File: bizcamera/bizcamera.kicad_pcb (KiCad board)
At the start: 2 copper layers, 84.5 x 55 mm, 0 parts

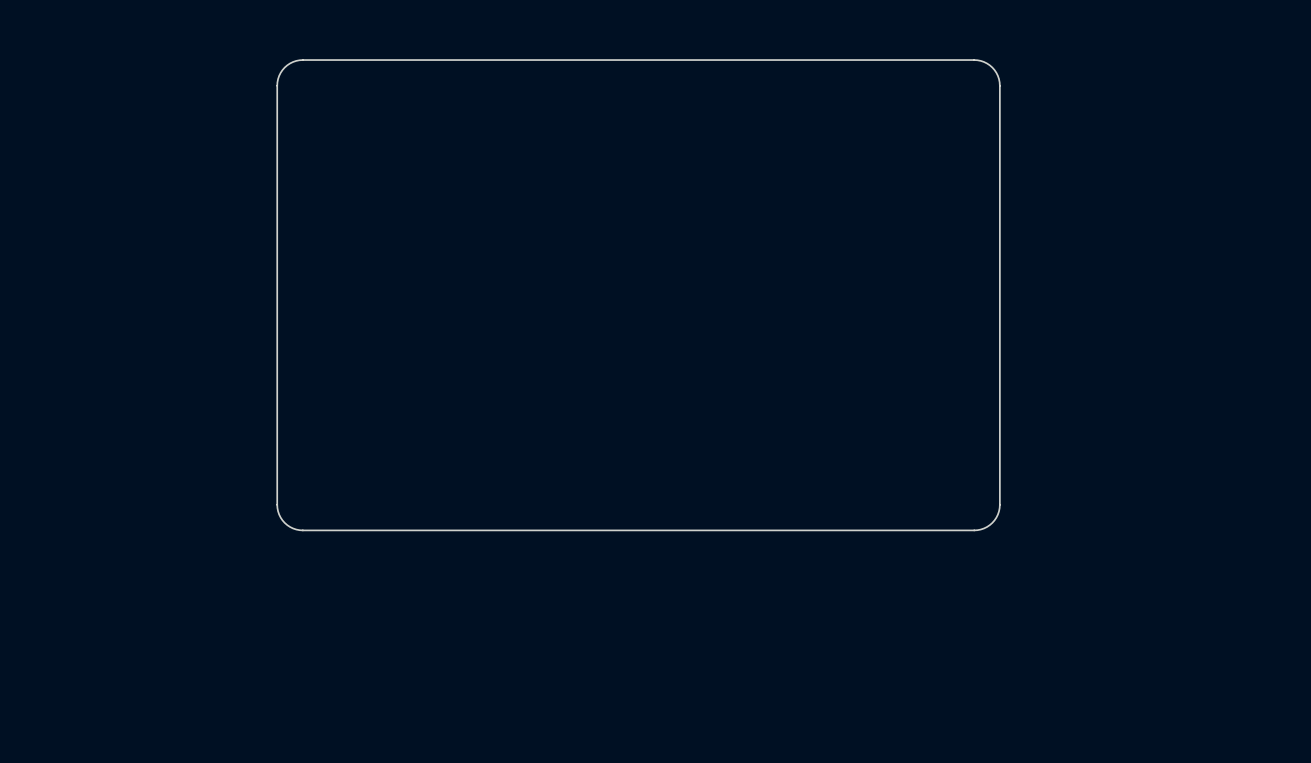
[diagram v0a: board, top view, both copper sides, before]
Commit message: Schematic rev1
Rev1 of the schematic, not finished, but close.

Switched to rp2350 because PIO is powerful enough to grab frames without DCMI iface
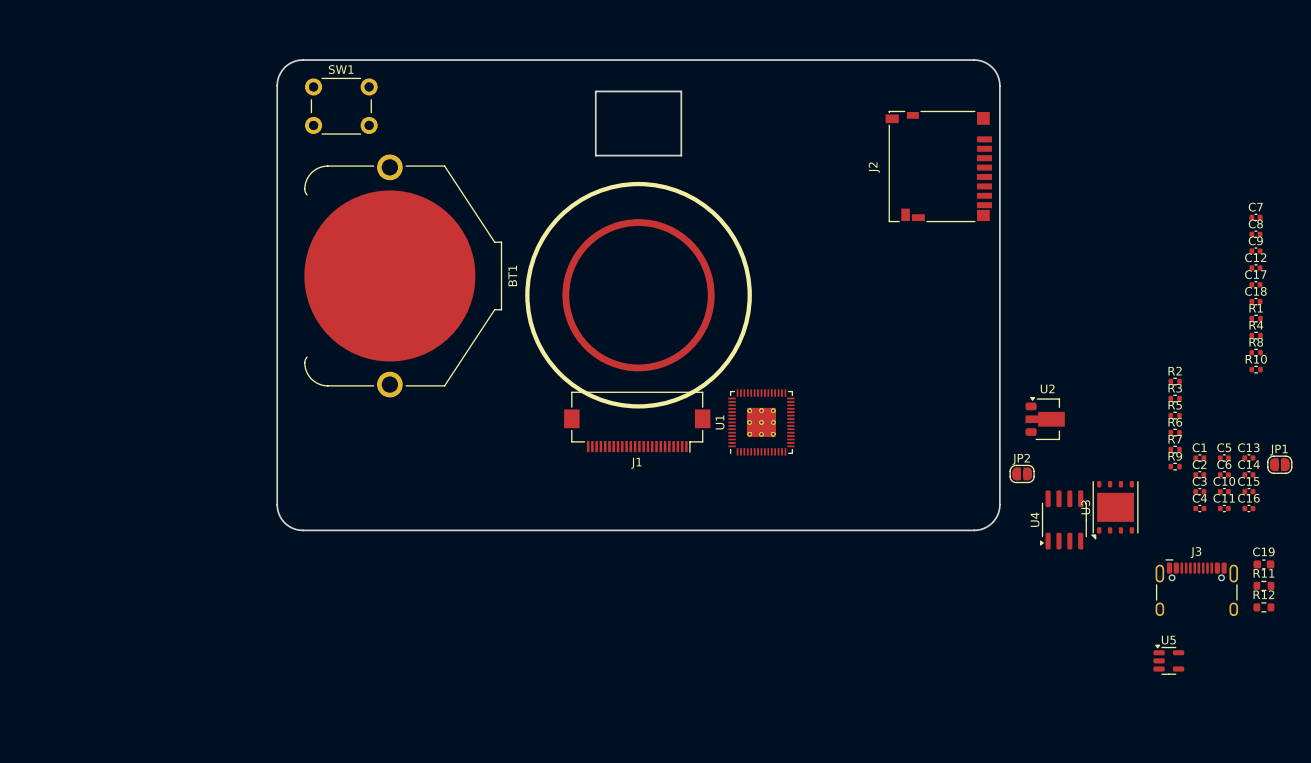
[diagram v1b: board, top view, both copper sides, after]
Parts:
- added BT1: CR2032, Battery:BatteryHolder_Keystone_3009_1x2450, F.Cu at (124.7, 90.2)
- added C1: 100n, Capacitor_SMD:C_0402_1005Metric, F.Cu at (219.4, 111.5)
- added C10: 100n, Capacitor_SMD:C_0402_1005Metric, F.Cu at (222.2, 115.5)
- added C11: 100n, Capacitor_SMD:C_0402_1005Metric, F.Cu at (222.2, 117.4)
- added C12: 4.7u, Capacitor_SMD:C_0402_1005Metric, F.Cu at (225.9, 89.3)
- added C13: 100n, Capacitor_SMD:C_0402_1005Metric, F.Cu at (225.1, 111.5)
- added C14: 100n, Capacitor_SMD:C_0402_1005Metric, F.Cu at (225.1, 113.5)
- added C15: 100n, Capacitor_SMD:C_0402_1005Metric, F.Cu at (225.1, 115.5)
- added C16: 100n, Capacitor_SMD:C_0402_1005Metric, F.Cu at (225.1, 117.4)
- added C17: 15p, Capacitor_SMD:C_0402_1005Metric, F.Cu at (225.9, 91.3)
- added C18: 15p, Capacitor_SMD:C_0402_1005Metric, F.Cu at (225.9, 93.2)
- added C19: 10u, Capacitor_SMD:C_0603_1608Metric, F.Cu at (226.9, 124.0)
- added C2: 100n, Capacitor_SMD:C_0402_1005Metric, F.Cu at (219.4, 113.5)
- added C3: 100n, Capacitor_SMD:C_0402_1005Metric, F.Cu at (219.4, 115.5)
- added C4: 100n, Capacitor_SMD:C_0402_1005Metric, F.Cu at (219.4, 117.4)
- added C5: 100n, Capacitor_SMD:C_0402_1005Metric, F.Cu at (222.2, 111.5)
- added C6: 100n, Capacitor_SMD:C_0402_1005Metric, F.Cu at (222.2, 113.5)
- added C7: 4.7u, Capacitor_SMD:C_0402_1005Metric, F.Cu at (225.9, 83.4)
- added C8: 4.7u, Capacitor_SMD:C_0402_1005Metric, F.Cu at (225.9, 85.4)
- added C9: 4.7u, Capacitor_SMD:C_0402_1005Metric, F.Cu at (225.9, 87.3)
- added J1: Camera, Connector_FFC-FPC:Hirose_FH12-24S-0.5SH_1x24-1MP_P0.50mm_Horizontal, F.Cu at (153.6, 108.3)
- added J2: Micro_SD_Card_Det1, Connector_Card:microSD_HC_Hirose_DM3D-SF, F.Cu at (188.8, 77.5)
- added J3: USB_C_Receptacle_USB2.0_14P, Connector_USB:USB_C_Receptacle_HCTL_HC-TYPE-C-16P-01A, F.Cu at (219.0, 128.2)
- added JP1: USB_BOOT, Jumper:SolderJumper-2_P1.3mm_Open_RoundedPad1.0x1.5mm, F.Cu at (228.7, 112.3)
- added JP2: USB_BOOT, Jumper:SolderJumper-2_P1.3mm_Open_RoundedPad1.0x1.5mm, F.Cu at (198.6, 113.4)
- added R1: 33, Resistor_SMD:R_0402_1005Metric, F.Cu at (226.0, 95.2)
- added R10: 10k, Resistor_SMD:R_0402_1005Metric, F.Cu at (226.0, 101.2)
- added R11: 5.1k, Resistor_SMD:R_0603_1608Metric, F.Cu at (226.9, 126.5)
- added R12: 5.1k, Resistor_SMD:R_0603_1608Metric, F.Cu at (226.9, 129.0)
- added R2: R, Resistor_SMD:R_0402_1005Metric, F.Cu at (216.5, 102.6)
- added R3: R, Resistor_SMD:R_0402_1005Metric, F.Cu at (216.5, 104.6)
- added R4: 1k, Resistor_SMD:R_0402_1005Metric, F.Cu at (226.0, 97.2)
- added R5: 0, Resistor_SMD:R_0402_1005Metric, F.Cu at (216.5, 106.6)
- added R6: 0, Resistor_SMD:R_0402_1005Metric, F.Cu at (216.5, 108.6)
- added R7: DNF, Resistor_SMD:R_0402_1005Metric, F.Cu at (216.5, 110.5)
- added R8: 1k, Resistor_SMD:R_0402_1005Metric, F.Cu at (226.0, 99.2)
- added R9: 0, Resistor_SMD:R_0402_1005Metric, F.Cu at (216.5, 112.5)
- added SW1: SW_Push, Button_Switch_THT:SW_PUSH_6mm_H4.3mm, F.Cu at (115.8, 68.2)
- added U1: RP2350_60QFN, RP2350A:RP2350-QFN-60-1EP_7x7_P0.4mm_EP3.4x3.4mm_ThermalVias, F.Cu at (168.1, 107.4)
- added U2: MCP1703Ax-180xxMB, Package_TO_SOT_SMD:SOT-89-3, F.Cu at (201.6, 107.0)
- added U3: W25Q128JVP, Package_SON:WSON-8-1EP_6x5mm_P1.27mm_EP3.4x4.3mm, F.Cu at (209.5, 117.3)
- added U4: ESP-PSRAM32, Package_SO:SOIC-8_3.9x4.9mm_P1.27mm, F.Cu at (203.5, 118.8)
- added U5: SPX3819M5-L-3-3, Package_TO_SOT_SMD:SOT-23-5, F.Cu at (215.8, 135.3)
- added kibuzzard-6812137D: G***, kibuzzard-6812137D, B.Cu at (171.9, 72.8)
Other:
- outline, holes or cut-outs redrawn

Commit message: Finish schematic
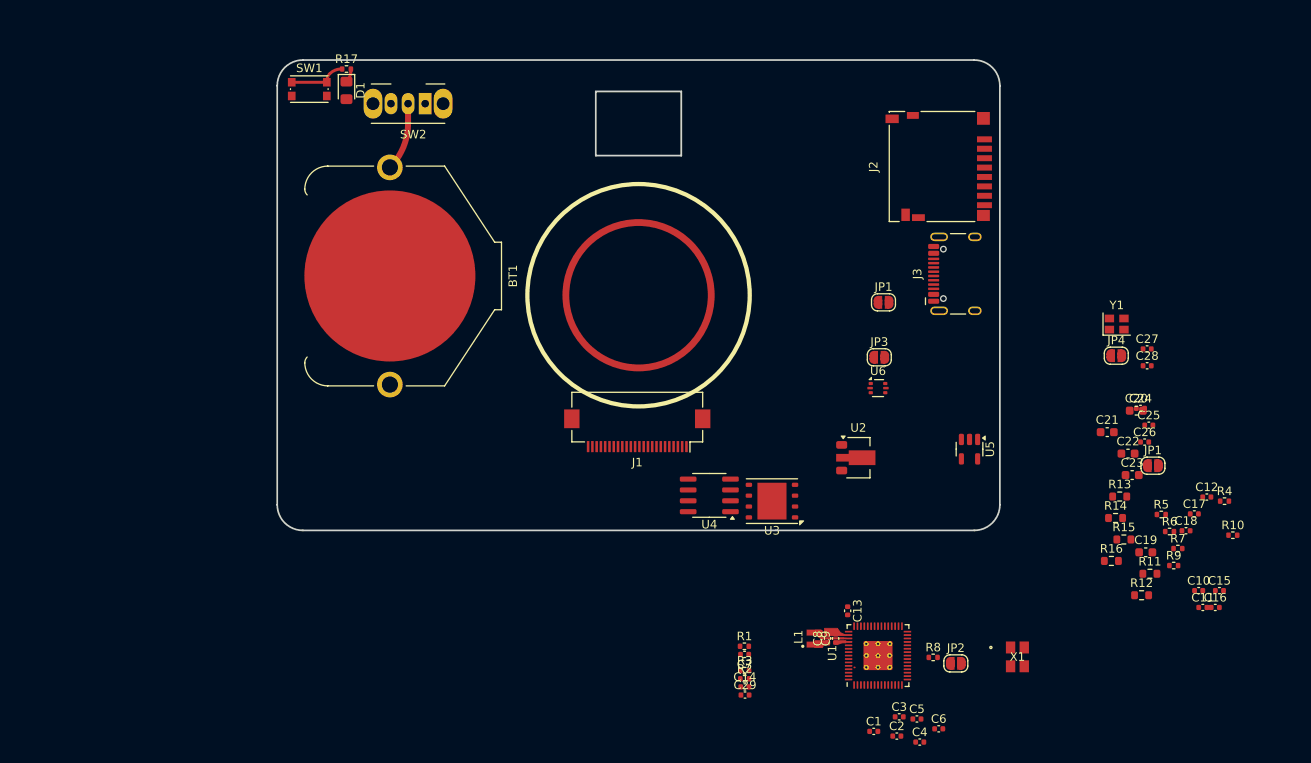
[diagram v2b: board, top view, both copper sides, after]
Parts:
- added C20: 10u, Capacitor_SMD:C_0603_1608Metric, F.Cu at (212.0, 106.0)
- added C21: 10u, Capacitor_SMD:C_0603_1608Metric, F.Cu at (208.6, 108.5)
- added C22: 10u, Capacitor_SMD:C_0603_1608Metric, F.Cu at (211.0, 111.0)
- added C23: 10u, Capacitor_SMD:C_0603_1608Metric, F.Cu at (211.5, 113.5)
- added C24: 100n, Capacitor_SMD:C_0402_1005Metric, F.Cu at (212.4, 105.7)
- added C25: 100n, Capacitor_SMD:C_0402_1005Metric, F.Cu at (213.4, 107.7)
- added C26: 15p, Capacitor_SMD:C_0402_1005Metric, F.Cu at (212.9, 109.7)
- added C27: 100n, Capacitor_SMD:C_0402_1005Metric, F.Cu at (213.2, 98.8)
- added C28: 100n, Capacitor_SMD:C_0402_1005Metric, F.Cu at (213.2, 100.8)
- added C29: 100n, Capacitor_SMD:C_0402_1005Metric, F.Cu at (166.2, 139.2)
- added D1: LED, LED_SMD:LED_0805_2012Metric_Pad1.15x1.40mm_HandSolder, F.Cu at (119.6, 68.5)
- added JP1: CAM_AF, Jumper:SolderJumper-2_P1.3mm_Open_RoundedPad1.0x1.5mm, F.Cu at (213.9, 112.4)
- added JP3: DVDD_1V8, Jumper:SolderJumper-2_P1.3mm_Open_RoundedPad1.0x1.5mm, F.Cu at (181.9, 99.8)
- added JP4: XTAL_JMP, Jumper:SolderJumper-2_P1.3mm_Open_RoundedPad1.0x1.5mm, F.Cu at (209.6, 99.6)
- added L1: 3.3u, RP2350A:L_pol_2016, F.Cu at (174.2, 132.7)
- added R13: 10K, Resistor_SMD:R_0603_1608Metric, F.Cu at (210.0, 116.0)
- added R14: 10K, Resistor_SMD:R_0603_1608Metric, F.Cu at (209.5, 118.5)
- added R15: 10K, Resistor_SMD:R_0603_1608Metric, F.Cu at (210.5, 121.1)
- added R16: 10K, Resistor_SMD:R_0603_1608Metric, F.Cu at (209.0, 123.6)
- added R17: 1k, Resistor_SMD:R_0402_1005Metric, F.Cu at (119.6, 66.0)
- added SW2: SW_SPDT, Button_Switch_THT:SW_Slide_SPDT_Angled_CK_OS102011MA1Q, F.Cu at (128.8, 70.1)
- added U6: USBLC6-2P6, Package_TO_SOT_SMD:SOT-666, F.Cu at (181.8, 103.4)
- added X1: ABM8-272-T3, ABM8_272_T3:ABM8-272-T3_ABR, F.Cu at (198.0, 134.8)
- added Y1: SG-210STF 24.0ML0, Oscillator:Oscillator_SMD_SeikoEpson_SG210-4Pin_2.5x2.0mm, F.Cu at (209.7, 95.9)
- C18: value 15p -> 12p
- J3: value USB_C_Receptacle_USB2.0_14P -> USB_IN
- JP1: value USB_BOOT -> CAM_AF
- R2, R3: value R -> 0
- R7: value DNF -> 10k
- SW1: value SW_Push -> USB_BOOT; footprint Button_Switch_THT:SW_PUSH_6mm_H4.3mm -> Button_Switch_SMD:SW_Push_1P1T_NO_CK_KMR2
- moved C7 78.7 mm to (166.2, 134.5), turned to 180 degrees
- moved R1 71.0 mm to (166.1, 133.6)
- moved C8 68.9 mm to (175.8, 132.6), turned to 90 degrees
- moved C9 66.8 mm to (176.8, 132.6), turned to 90 degrees
- moved C14 63.9 mm to (166.2, 138.3)
- moved R2 61.2 mm to (166.2, 137.3)
- moved R3 59.5 mm to (166.2, 136.4)
- moved R8 51.9 mm to (188.2, 134.8)
- moved C13 50.2 mm to (178.2, 129.4), turned to -90 degrees
- moved JP1 50.1 mm to (182.4, 93.3)
- moved C1 49.8 mm to (181.2, 143.5)
- moved C5 47.2 mm to (186.3, 142.1)
- moved C2 46.8 mm to (183.9, 144.1)
- moved J3 46.8 mm to (192.0, 90.0), turned to 90 degrees
- moved C6 44.7 mm to (188.8, 143.2)
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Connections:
- BT1 pad 1: +3V3 -> Net-(BT1-+)
- C18 pad 1: unconnected-(C18-Pad1) -> /XIN
- C19 pad 1: +5V -> -BATT
- C19 pad 2: -BATT -> +5V
- J1 pad 12: /MCLK -> /CAM_XTAL
- J1 pad 14: /DOVDD 1.8 -> +1V8
- J1 pad 2: +3V3 -> Net-(J1-Pin_2)
- J3 pad A6: /USB_DP -> Net-(J3-D+-PadA6)
- J3 pad A7: /USB_DM -> Net-(J3-D--PadA7)
- J3 pad B6: /USB_DP -> Net-(J3-D+-PadA6)
- J3 pad B7: /USB_DM -> Net-(J3-D--PadA7)
- JP1 pad 1: -BATT -> +3V3
- JP1 pad 2: /USB_BOOT -> Net-(J1-Pin_2)
- JP2 pad 2: Net-(JP2-B) -> -BATT
- R2 pad 1: Net-(U1-USB_DP) -> /USB_DP
- R3 pad 1: Net-(U1-USB_DM) -> /USB_DN
- R3 pad 2: /USB_DM -> /USB_DN
- R8 pad 1: -BATT -> Net-(U1-RUN)
- R8 pad 2: Net-(JP2-B) -> Net-(JP2-A)
- SW1 pad 1: unconnected-(SW1-Pad1) -> -BATT
- SW1 pad 2: unconnected-(SW1-Pad2) -> /USB_BOOT
- U1 pad 10: unconnected-(U1-GPIO7-Pad10) -> /D3
- U1 pad 12: unconnected-(U1-GPIO8-Pad12) -> /D4/MDN0
- U1 pad 13: unconnected-(U1-GPIO9-Pad13) -> /SDA
- U1 pad 14: unconnected-(U1-GPIO10-Pad14) -> /SCL
- U1 pad 15: unconnected-(U1-GPIO11-Pad15) -> /RST
- U1 pad 16: unconnected-(U1-GPIO12-Pad16) -> /VSYNC
- U1 pad 17: unconnected-(U1-GPIO13-Pad17) -> /HSYNC
- U1 pad 18: unconnected-(U1-GPIO14-Pad18) -> /PCLK
- U1 pad 26: Net-(JP2-A) -> Net-(U1-RUN)
- U1 pad 28: unconnected-(U1-GPIO17-Pad28) -> /XTAL_EN
- U1 pad 3: unconnected-(U1-GPIO1-Pad3) -> /D9/MPD1
- U1 pad 31: unconnected-(U1-GPIO19-Pad31) -> /SD_DET
- U1 pad 32: unconnected-(U1-GPIO20-Pad32) -> /SPI_DO
- U1 pad 33: unconnected-(U1-GPIO21-Pad33) -> /SCLK
- U1 pad 34: unconnected-(U1-GPIO22-Pad34) -> /SPI_DI
- U1 pad 35: unconnected-(U1-GPIO23-Pad35) -> /SPI_CS
- U1 pad 36: unconnected-(U1-GPIO24-Pad36) -> Net-(D1-A)
- U1 pad 4: unconnected-(U1-GPIO2-Pad4) -> /D8/MDN1
- U1 pad 5: unconnected-(U1-GPIO3-Pad5) -> /D7/MCP
- U1 pad 51: Net-(U1-USB_DM) -> /USB_DN
- U1 pad 52: Net-(U1-USB_DP) -> /USB_DP
- U1 pad 54: unconnected-(U1-QSPI_IOVDD-Pad54) -> +3V3
- U1 pad 7: unconnected-(U1-GPIO4-Pad7) -> /D6/MCN
- U1 pad 8: unconnected-(U1-GPIO5-Pad8) -> /D2
- U1 pad 9: unconnected-(U1-GPIO6-Pad9) -> /D5/MDP0
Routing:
- net Net-(BT1-+): track 0.00 -> 7.98 mm
- net -BATT: track 0.00 -> 6.77 mm
- net Net-(D1-K): track 0.00 -> 1.60 mm

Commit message: Near final design
Near final design for prototype model, for both schematic and PCB

Layout was an absolute nightmare. But I think this is the best I can do with the constraints, and it should look pretty nice too.
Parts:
- removed the JP1 at (213.9, 112.4)
- removed SW2: SW_SPDT, Button_Switch_THT:SW_Slide_SPDT_Angled_CK_OS102011MA1Q
- removed kibuzzard-6812137D: G***, kibuzzard-6812137D
- added C30: 10u, Capacitor_SMD:C_0603_1608Metric, F.Cu at (123.5, 112.5)
- added C31: 68u, Capacitor_SMD:C_0603_1608Metric, F.Cu at (129.8, 114.6)
- added C32: 68u, Capacitor_SMD:C_0603_1608Metric, F.Cu at (128.4, 114.6)
- added C33: 10u, Capacitor_SMD:C_0603_1608Metric, F.Cu at (141.5, 113.0)
- added C34: 10u, Capacitor_SMD:C_0603_1608Metric, F.Cu at (140.0, 113.0)
- added C35: 10u, Capacitor_SMD:C_0603_1608Metric, F.Cu at (137.7, 110.5)
- added L2: 1u, Kiyo:TFM201610ALMA, F.Cu at (123.9, 114.6)
- added L3: 1u, Kiyo:TFM201610ALMA, F.Cu at (138.9, 115.9)
- added R18: 10k, Resistor_SMD:R_0402_1005Metric, F.Cu at (185.5, 106.1)
- added R19: 453k, Resistor_SMD:R_0402_1005Metric_Pad0.72x0.64mm_HandSolder, F.Cu at (129.1, 112.0)
- added REF**: BatteryHolder_Keystone_2468_2xAAA, Battery:BatteryHolder_Keystone_2468_2xAAA, F.Cu at (89.1, 116.6)
- added SW3: Shutter, Button_Switch_SMD:SW_Push_1P1T_NO_6x6mm_H9.5mm, F.Cu at (117.9, 70.2)
- added U7: TPS61022, Package_DFN_QFN:Texas_RWU0007A_VQFN-7_2x2mm_P0.5mm, F.Cu at (126.3, 113.2)
- added U8: TPS628437DRL, Package_TO_SOT_SMD:SOT-563, F.Cu at (138.3, 113.3)
- added kibuzzard-6824811E: G***, kibuzzard-6824811E, B.Cu at (165.6, 72.5)
- added kibuzzard-68248180: G***, kibuzzard-68248180, B.Cu at (131.6, 68.4)
- added kibuzzard-6825B58C: G***, kibuzzard-6825B58C, F.Cu at (118.0, 78.5)
- D1: footprint LED_SMD:LED_0805_2012Metric_Pad1.15x1.40mm_HandSolder -> LED_SMD:LED_1206_3216Metric_ReverseMount_Hole1.8x2.4mm
- R6: value 0 -> 100k; footprint Resistor_SMD:R_0402_1005Metric -> Resistor_SMD:R_0402_1005Metric_Pad0.72x0.64mm_HandSolder
- U2: value MCP1703Ax-180xxMB -> SPX3819M5-L-1-8; footprint Package_TO_SOT_SMD:SOT-89-3 -> Package_TO_SOT_SMD:SOT-23-5
- U3: value W25Q128JVP -> S25FS128SDSNFI101
- U4: value ESP-PSRAM32 -> ESP-PSRAM64
- moved R6 88.1 mm to (128.1, 112.0), turned to -90 degrees
- moved C27 71.0 mm to (143.3, 111.0), turned to 180 degrees
- moved C28 70.5 mm to (143.3, 110.0)
- moved C25 65.5 mm to (148.2, 113.2), turned to 90 degrees
- moved SW1 63.6 mm to (169.8, 101.1), turned to 90 degrees
- moved R16 62.8 mm to (147.0, 113.8), turned to 90 degrees
- moved C15 62.4 mm to (175.6, 85.0), turned to 180 degrees
- moved R15 61.5 mm to (149.4, 113.8), turned to 90 degrees
- moved C16 60.4 mm to (175.6, 89.4), turned to -90 degrees
- moved R14 58.8 mm to (150.9, 113.8), turned to 90 degrees
- moved C26 56.9 mm to (156.1, 113.1), turned to 90 degrees
- moved R13 56.7 mm to (153.4, 113.6), turned to 90 degrees
- moved R10 53.4 mm to (173.5, 101.0)
- moved R4 51.6 mm to (173.5, 99.8)
- moved C10 50.7 mm to (174.1, 103.9), turned to 180 degrees
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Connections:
- BT1 pad 1: Net-(BT1-+) -> +BATT
- C15 pad 2: +3V3 -> +1V8
- C16 pad 2: +3V3 -> +1V8
- C22 pad 1: +3V3 -> +5V
- J3 pad A6: Net-(J3-D+-PadA6) -> /USB_DP
- J3 pad A7: Net-(J3-D--PadA7) -> /USB_DN
- J3 pad B6: Net-(J3-D+-PadA6) -> /USB_DP
- J3 pad B7: Net-(J3-D--PadA7) -> /USB_DN
- R10 pad 2: +3V3 -> +1V8
- R6 pad 1: /GPIO0 -> -BATT
- R6 pad 2: Net-(U3-~{CS}) -> Net-(U7-FB)
- R7 pad 2: +3V3 -> +1V8
- U1 pad 10: /D3 -> unconnected-(U1-GPIO7-Pad10)
- U1 pad 12: /D4/MDN0 -> /D7/MCP
- U1 pad 13: /SDA -> /D8/MDN1
- U1 pad 14: /SCL -> /D9/MPD1
- U1 pad 15: /RST -> /HSYNC
- U1 pad 17: /HSYNC -> /RST
- U1 pad 18: /PCLK -> /SCL
- U1 pad 19: unconnected-(U1-GPIO15-Pad19) -> /SDA
- U1 pad 3: /D9/MPD1 -> /D4/MDN0
- U1 pad 31: /SD_DET -> /SPI_DO
- U1 pad 32: /SPI_DO -> /SCLK
- U1 pad 33: /SCLK -> /SPI_DI
- U1 pad 34: /SPI_DI -> /SPI_CS
- U1 pad 35: /SPI_CS -> /SD_DET
- U1 pad 37: unconnected-(U1-GPIO25-Pad37) -> Net-(U1-GPIO25)
- U1 pad 4: /D8/MDN1 -> /D3
- U1 pad 5: /D7/MCP -> /D5/MDP0
- U1 pad 7: /D6/MCN -> /D2
- U1 pad 8: /D2 -> /D6/MCN
- U1 pad 9: /D5/MDP0 -> /PCLK
- U2 pad 1: -BATT -> +5V
- U2 pad 2: +3V3 -> -BATT
- U2 pad 3: +1V8 -> +5V
- U3 pad 8: +3V3 -> +1V8
- U4 pad 2: /QSPI_SD3 -> /QSPI_SD1
- U4 pad 3: /QSPI_SD1 -> /QSPI_SD2
- U4 pad 5: /QSPI_SD2 -> /QSPI_SD0
- U4 pad 7: /QSPI_SD0 -> /QSPI_SD3
- U4 pad 8: +3V3 -> +1V8
- U6 pad 3: /USB_DM -> /USB_DN
- U6 pad 4: Net-(J3-D--PadA7) -> /USB_DN
- U6 pad 6: Net-(J3-D+-PadA6) -> /USB_DP
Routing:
- net +1V8: track 0.00 -> 244.6 mm, vias 0 -> 11
- net -BATT: track 6.77 -> 133.7 mm, vias 0 -> 23
- net Net-(U1-GPIO25): track 0.00 -> 89.2 mm, vias 0 -> 2
- net Net-(D1-A): track 0.00 -> 74.2 mm, vias 0 -> 2
- net +BATT: track 0.00 -> 48.1 mm
- net +1V1: track 0.00 -> 46.4 mm, vias 0 -> 4
- net /SDA: track 0.00 -> 43.2 mm
- net /SPI_CS: track 0.00 -> 40.0 mm
- net /SPI_DI: track 0.00 -> 39.5 mm
- net /SCL: track 0.00 -> 39.0 mm
- net /SCLK: track 0.00 -> 37.4 mm
- net /SD_DET: track 0.00 -> 36.7 mm
- net /RST: track 0.00 -> 36.2 mm
- net /SPI_DO: track 0.00 -> 35.6 mm
- net /VSYNC: track 0.00 -> 34.9 mm
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- added copper zone on F.Cu, net +1V8
- added copper zone on In2.Cu, net +3V3
- added copper zone on F.Cu, net +BATT
- added copper zone on B.Cu, net -BATT
- added copper zone on F.Cu, net -BATT
- added copper zone on In1.Cu, net -BATT
- added copper zone on F.Cu, net Net-(U7-SW)
- added copper zone on F.Cu, net Net-(U8-SW)
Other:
- copper layers 2 -> 4

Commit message: Tidy up
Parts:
- removed REF**: BatteryHolder_Keystone_2468_2xAAA, Battery:BatteryHolder_Keystone_2468_2xAAA
